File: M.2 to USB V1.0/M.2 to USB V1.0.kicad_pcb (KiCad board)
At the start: 2 copper layers, 22 x 26 mm, 29 parts, among them IC1 USB2422T_MJ, IC2 TPS2041CDBVT, IC3 TPS2041CDBVT, J1 M.2 Slot, J2 Conn_2Rows-09Pins, U1 APX809-46SRG-7, Y1 RH100-24.000-9-1015-EXT-TR

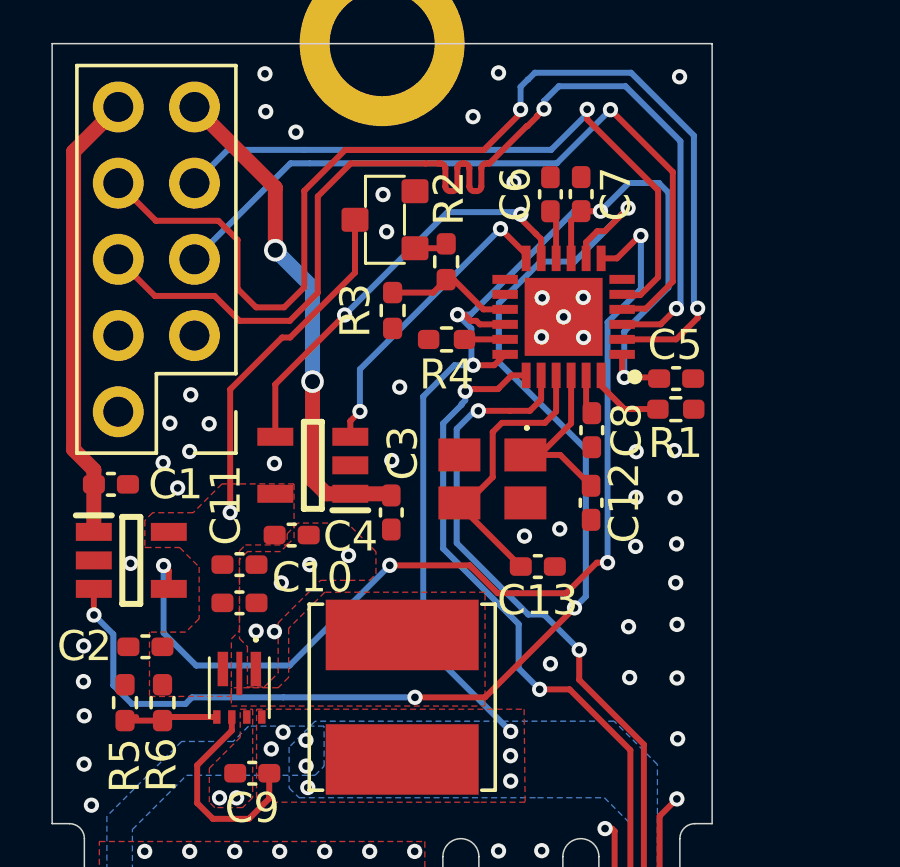
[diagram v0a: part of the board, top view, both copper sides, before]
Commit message: updated pcb
updated pcb

calculated load caps

added 3D render
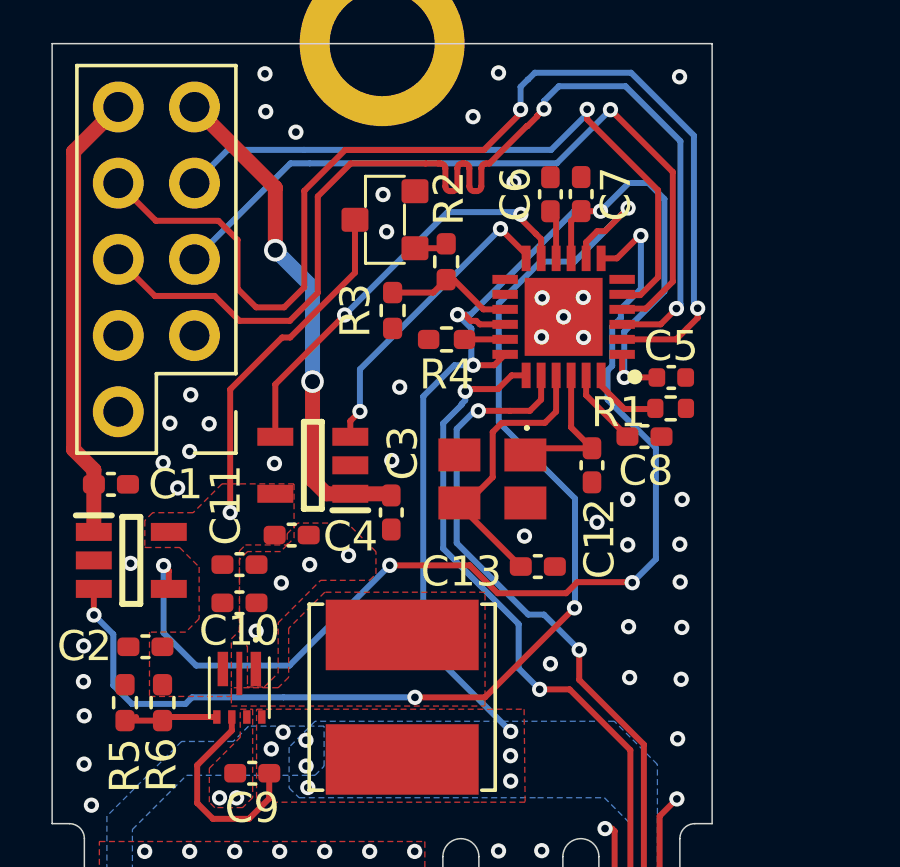
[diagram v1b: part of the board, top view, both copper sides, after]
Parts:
- C5: footprint Capacitor_SMD:C_0402_1005Metric_Pad0.74x0.62mm_HandSolder -> Capacitor_SMD:C_0402_1005Metric
- R1: footprint Resistor_SMD:R_0402_1005Metric_Pad0.72x0.64mm_HandSolder -> Resistor_SMD:R_0402_1005Metric
- moved C8 1.77 mm to (163.6, 81.5), turned to 0 degrees
- moved C12 1.25 mm to (161.9, 82.5)
- moved R1 0.17 mm to (164.5, 80.6)
- moved C5 0.17 mm to (164.5, 79.6)
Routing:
- net Port1_EN: track 33.6 -> 35.8 mm
- net Net-(IC1-PLLFILT): track 1.34 -> 2.61 mm
- net XTAL1: track 6.18 -> 5.51 mm
- net GND: vias 62 -> 59

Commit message: updated pcb
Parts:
- added G***: LOGO, LOGO, F.Cu at (162.4, 90.5)
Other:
- board text added: "(symbol "LOGO" (pin_names (offset 1.016)) (in_bom yes) (on_board yes) (property "Reference" "#G" (at 0 2.11501 0) (effects (font (size 1.27 1.27)) hide) ) (property "Value" "LOGO" (at 0 -2.11501 0) (effects (font (size 1.27 1.27)) hide) ) (property "Footprint" "" (at 0 0 0) (effects (font (size 1.27 1.27)) hide) ) (property "Datasheet" "" (at 0 0 0) (effects (font (size 1.27 1.27)) hide) ) (symbo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"

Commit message: fixed copper pour bug
bug caused by this (https://gitlab.com/kicad/code/kicad/-/issues?show=eyJpaWQiOiIyMDY5NiIsImZ1bGxfcGF0aCI6ImtpY2FkL2NvZGUva2ljYWQiLCJpZCI6MTY2MjEzNzM2fQ%3D%3D) caused copper pours to be corrupted. this updated fixes that.
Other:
- board text removed: "(symbol "LOGO" (pin_names (offset 1.016)) (in_bom yes) (on_board yes) (property "Reference" "#G" (at 0 2.11501 0) (effects (font (size 1.27 1.27)) hide) ) (property "Value" "LOGO" (at 0 -2.11501 0) (effects (font (size 1.27 1.27)) hide) ) (property "Footprint" "" (at 0 0 0) (effects (font (size 1.27 1.27)) hide) ) (property "Datasheet" "" (at 0 0 0) (effects (font (size 1.27 1.27)) hide) ) (symbo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"

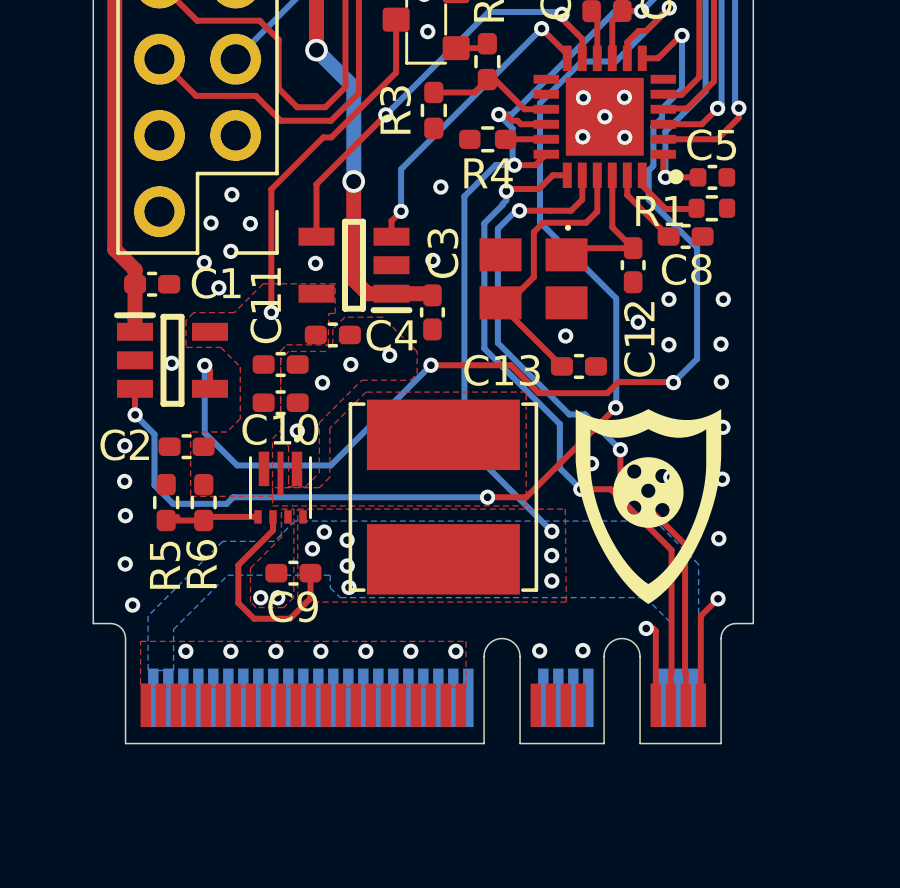
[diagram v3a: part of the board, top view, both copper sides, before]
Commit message: fixed missing ground connection
pin 18 was not connected to ground net. it is now connected.
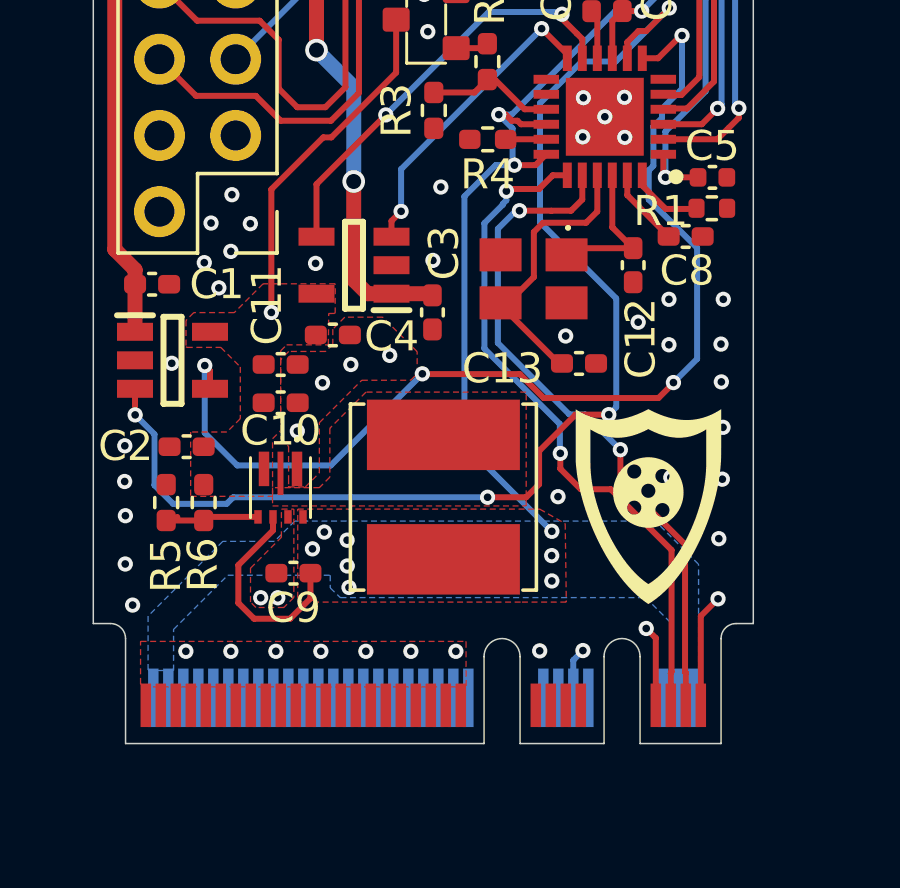
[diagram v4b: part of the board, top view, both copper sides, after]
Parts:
- moved C13 0.10 mm to (160.1, 85.8)
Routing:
- net GND: track 6.62 -> 8.19 mm
- net OC1: track 39.7 -> 40.3 mm
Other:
- board text added: "M.2 to USB V1.0 By SuperCookie"
